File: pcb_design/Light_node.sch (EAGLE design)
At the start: 38 parts, among them U10 MCP73831T-2ACI/OT, U20 LIS3DHTR, U30 ATmega328P, U40 MIC5225-3.3v, U50 COMMON_ANODE_DIODE, Y30 12MHz

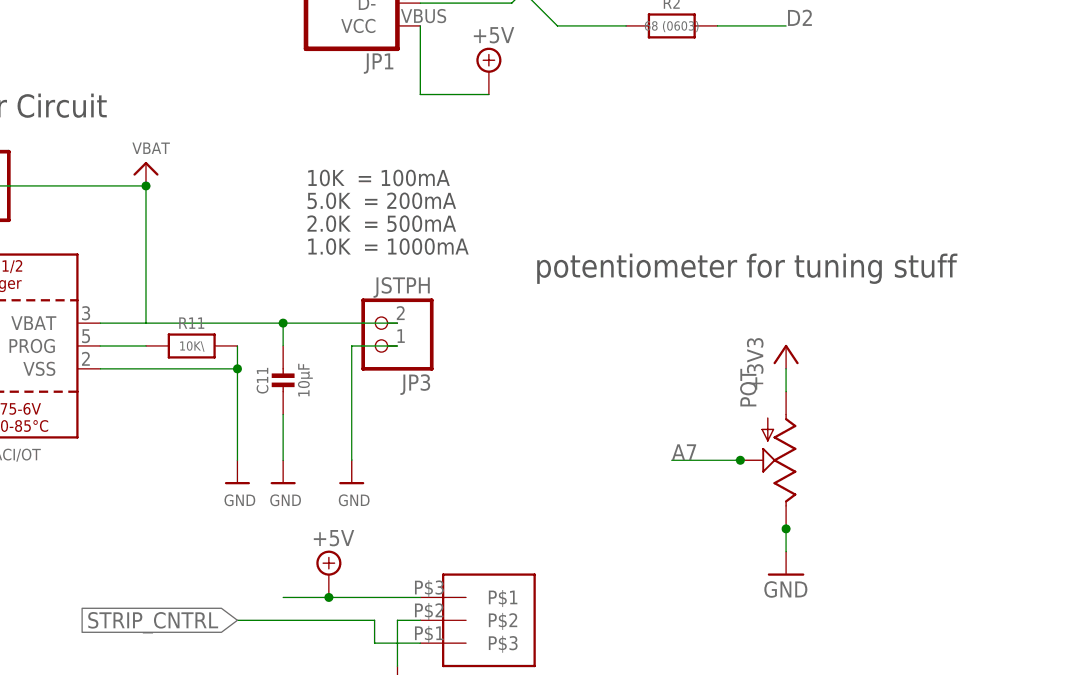
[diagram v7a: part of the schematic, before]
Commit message: added the switch to the bottom
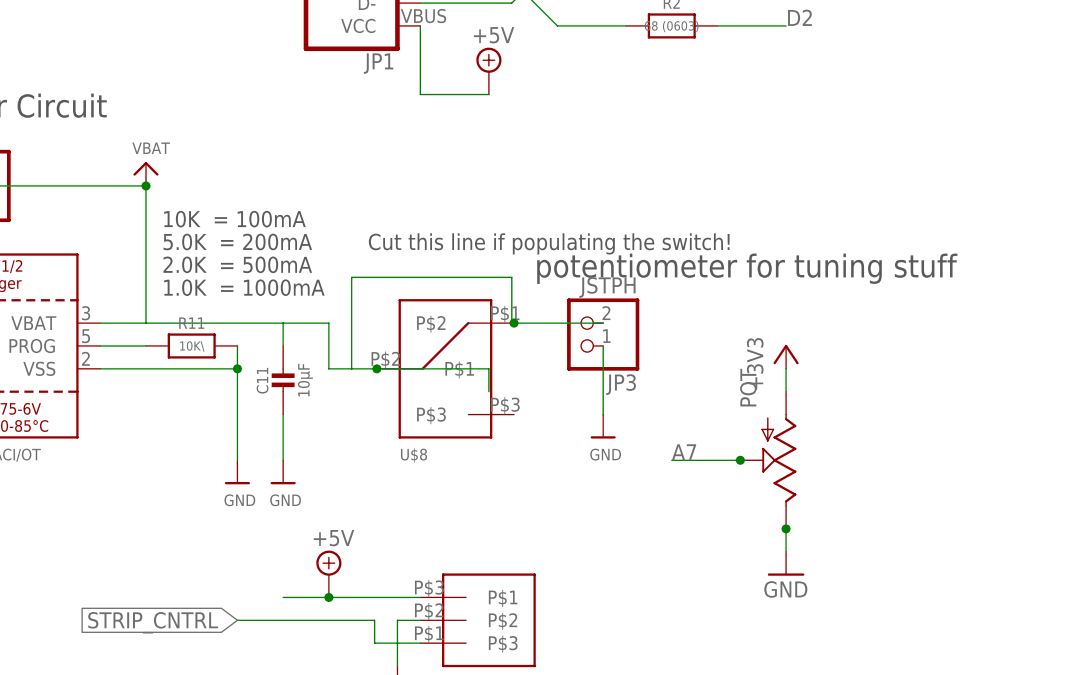
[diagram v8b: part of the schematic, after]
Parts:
- added U$8: SPDT_NO_GNDSMT, 0_Shibbs1:SPDT_NO_GNDSMT
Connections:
- net VBAT: now also U$8.P$1, U$8.P$2
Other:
- note added: "Cut this line if populating the switch!"
- moved on the sheet: JP3
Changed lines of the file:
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@@
 <layer number="56" name="wert" color="7" fill="1" visible="no" active="no"/>
 <layer number="57" name="tCAD" color="7" fill="1" visible="no" active="no"/>
+<layer number="59" name="tCarbon" color="7" fill="1" visible="no" active="no"/>
+<layer number="60" name="bCarbon" color="7" fill="1" visible="no" active="no"/>
 <layer number="90" name="Modules" color="7" fill="1" visible="no" active="yes"/>
 <layer number="91" name="Nets" color="2" fill="1" visible="yes" active="yes"/>
@@
 <layer number="127" name="_tValues" color="7" fill="1" visible="yes" active="yes"/>
 <layer number="128" name="_bValues" color="7" fill="1" visible="yes" active="yes"/>
+<layer number="129" name="Mask" color="7" fill="1" visible="yes" active="yes"/>
 <layer number="131" name="tAdjust" color="7" fill="1" visible="no" active="yes"/>
 <layer number="132" name="bAdjust" color="7" fill="1" visible="no" active="yes"/>
@@
 <layer number="227" name="227bmp" color="7" fill="1" visible="yes" active="yes"/>
 <layer number="228" name="228bmp" color="7" fill="1" visible="yes" active="yes"/>
+<layer number="229" name="229bmp" color="7" fill="1" visible="yes" active="yes"/>
+<layer number="230" name="230bmp" color="7" fill="1" visible="yes" active="yes"/>
 <layer number="231" name="Eagle3D_PG1" color="7" fill="1" visible="no" active="no"/>
 <layer number="232" name="Eagle3D_PG2" color="7" fill="1" visible="no" active="no"/>
@@
 <layer number="251" name="SMDround" color="7" fill="1" visible="no" active="no"/>
 <layer number="254" name="cooling" color="7" fill="1" visible="yes" active="yes"/>
+<layer number="255" name="routoute" color="7" fill="1" visible="yes" active="yes"/>
 </layers>
 <schematic>
@@
 <part name="U$5" library="microbuilder" deviceset="GND" device=""/>
 <part name="C11" library="microbuilder" deviceset="CAP_CERAMIC" device="0805-NOOUTLINE" value="10µF"/>
-<part name="U$10" library="microbuilder" deviceset="GND" device=""/>
 <part name="U$11" library="microbuilder" deviceset="GND" device=""/>
 <part name="R11" library="microbuilder" deviceset="RESISTOR" device="0805_NOOUTLINE" value="10K\"/>
@@
 <part name="SUPPLY8" library="supply2" deviceset="+5V" device=""/>
 <part name="U$1" library="microbuilder" deviceset="GND" device=""/>
+<part name="U$8" library="0_Shibbs1" deviceset="SPDT_NO_GND" device="SMT"/>
+<part name="U$9" library="microbuilder" deviceset="GND" device=""/>
 </parts>
 <sheets>
@@
 <text x="175.26" y="25.4" size="2.54" layer="94">http://adafruit.com/products/2010</text>
 <text x="248.92" y="30.48" size="2.54" layer="94">CC 2.5 BY-SA</text>
-<text x="205.74" y="160.02" size="1.778" layer="97">10K  = 100mA</text>
-<text x="205.74" y="157.48" size="1.778" layer="97">5.0K  = 200mA</text>
-<text x="205.74" y="154.94" size="1.778" layer="97">2.0K  = 500mA</text>
-<text x="205.74" y="152.4" size="1.778" layer="97">1.0K  = 1000mA</text>
+<text x="189.738" y="155.448" size="1.778" layer="97">10K  = 100mA</text>
+<text x="189.738" y="152.908" size="1.778" layer="97">5.0K  = 200mA</text>
+<text x="189.738" y="150.368" size="1.778" layer="97">2.0K  = 500mA</text>
+<text x="189.738" y="147.828" size="1.778" layer="97">1.0K  = 1000mA</text>
 <text x="147.32" y="167.64" size="2.54" layer="97">Battery Charger Circuit</text>
 <text x="15.24" y="198.12" size="2.54" layer="97">USB power LED</text>
@@
 Short JP5 and DNP the lithium battery. If you don't do this things are going to get fucked up</text>
 <text x="68.58" y="104.14" size="2.54" layer="97">BAW56L </text>
+<text x="212.598" y="152.908" size="1.778" layer="97">Cut this line if populating the switch!</text>
 </plain>
 <instances>
@@
 <instance part="CH_LED" gate="G$1" x="134.62" y="132.08" rot="R180"/>
 <instance part="R10" gate="G$1" x="147.32" y="132.08"/>
-<instance part="JP3" gate="G$1" x="213.36" y="144.78" rot="R180"/>
+<instance part="JP3" gate="G$1" x="236.22" y="144.78" rot="R180"/>
 <instance part="C10" gate="G$1" x="121.92" y="137.16"/>
 <instance part="U$5" gate="G$1" x="121.92" y="127"/>
 <instance part="C11" gate="G$1" x="203.2" y="137.16"/>
-<instance part="U$10" gate="G$1" x="210.82" y="127"/>
 <instance part="U$11" gate="G$1" x="203.2" y="127"/>
 <instance part="R11" gate="G$1" x="193.04" y="142.24"/>
@@
 <instance part="SUPPLY8" gate="+5V" x="226.06" y="172.72"/>
 <instance part="U$1" gate="G$1" x="226.06" y="185.42"/>
+<instance part="U$8" gate="G$1" x="221.234" y="139.7"/>
+<instance part="U$9" gate="G$1" x="238.76" y="132.08"/>
 </instances>
 <busses>
@@
 </segment>
 <segment>
-<pinref part="U$10" gate="G$1" pin="GND"/>
-<wire x1="210.82" y1="142.24" x2="210.82" y2="129.54" width="0.1524" layer="91"/>
-<pinref part="JP3" gate="G$1" pin="1"/>
-<wire x1="210.82" y1="142.24" x2="215.9" y2="142.24" width="0.1524" layer="91"/>
-</segment>
-<segment>
 <pinref part="C11" gate="G$1" pin="2"/>
 <pinref part="U$11" gate="G$1" pin="GND"/>
@@
 <pinref part="U$1" gate="G$1" pin="GND"/>
 <wire x1="226.06" y1="187.96" x2="218.44" y2="187.96" width="0.1524" layer="91"/>
+</segment>
+<segment>
+<pinref part="JP3" gate="G$1" pin="1"/>
+<pinref part="U$9" gate="G$1" pin="GND"/>
+<wire x1="238.76" y1="134.62" x2="238.76" y2="142.24" width="0.1524" layer="91"/>
 </segment>
 </net>
@@
 <wire x1="187.96" y1="144.78" x2="182.88" y2="144.78" width="0.1524" layer="91"/>
 <wire x1="203.2" y1="142.24" x2="203.2" y2="144.78" width="0.1524" layer="91"/>
-<pinref part="JP3" gate="G$1" pin="2"/>
-<wire x1="203.2" y1="144.78" x2="215.9" y2="144.78" width="0.1524" layer="91"/>
-<junction x="203.2" y="144.78"/>
 <pinref part="JP11" gate="G$1" pin="2"/>
 <wire x1="170.18" y1="160.02" x2="187.96" y2="160.02" width="0.1524" layer="91"/>
@@
 <pinref part="U$14" gate="G$1" pin="VBAT"/>
 <junction x="187.96" y="160.02"/>
-</segment>
-<segment>
+<wire x1="213.36" y1="139.7" x2="213.614" y2="139.7" width="0.1524" layer="91"/>
+<wire x1="213.614" y1="139.7" x2="210.82" y2="139.7" width="0.1524" layer="91"/>
+<wire x1="210.82" y1="139.7" x2="208.28" y2="139.7" width="0.1524" layer="91"/>
+<wire x1="208.28" y1="139.7" x2="208.28" y2="144.78" width="0.1524" layer="91"/>
+<wire x1="208.28" y1="144.78" x2="203.2" y2="144.78" width="0.1524" layer="91"/>
+<pinref part="U$8" gate="G$1" pin="P$1"/>
+<junction x="213.614" y="139.7"/>
+<wire x1="238.76" y1="144.78" x2="228.854" y2="144.78" width="0.1524" layer="91"/>
+<wire x1="228.854" y1="144.78" x2="228.6" y2="144.78" width="0.1524" layer="91"/>
+<wire x1="228.6" y1="144.78" x2="228.6" y2="149.86" width="0.1524" layer="91"/>
+<pinref part="JP3" gate="G$1" pin="2"/>
+<pinref part="U$8" gate="G$1" pin="P$2"/>
+<junction x="228.854" y="144.78"/>
+<wire x1="228.6" y1="149.86" x2="210.82" y2="149.86" width="0.1524" layer="91"/>
+<wire x1="210.82" y1="149.86" x2="210.82" y2="139.7" width="0.1524" layer="91"/>
+<wire x1="213.614" y1="139.7" x2="226.06" y2="139.7" width="0.1524" layer="91"/>
+<wire x1="226.06" y1="139.7" x2="226.06" y2="137.16" width="0.1524" layer="91"/>
+</segment>
+<segment>
